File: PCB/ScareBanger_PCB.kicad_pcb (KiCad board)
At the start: 2 copper layers, 76 x 56 mm, 15 parts, among them J1 RJ45, J16 Conn_01x10_Female - SAINSMART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, J17 Screw_Terminal_01x10 - HILETG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, J2 1757271, J3 Screw_Terminal_01x06, J4 Barrel_Jack_Switch, J6 Screw_Terminal_01x06, J7 Screw_Terminal_01x06, SW1 SW_SPDT, SW2 SW_SPDT

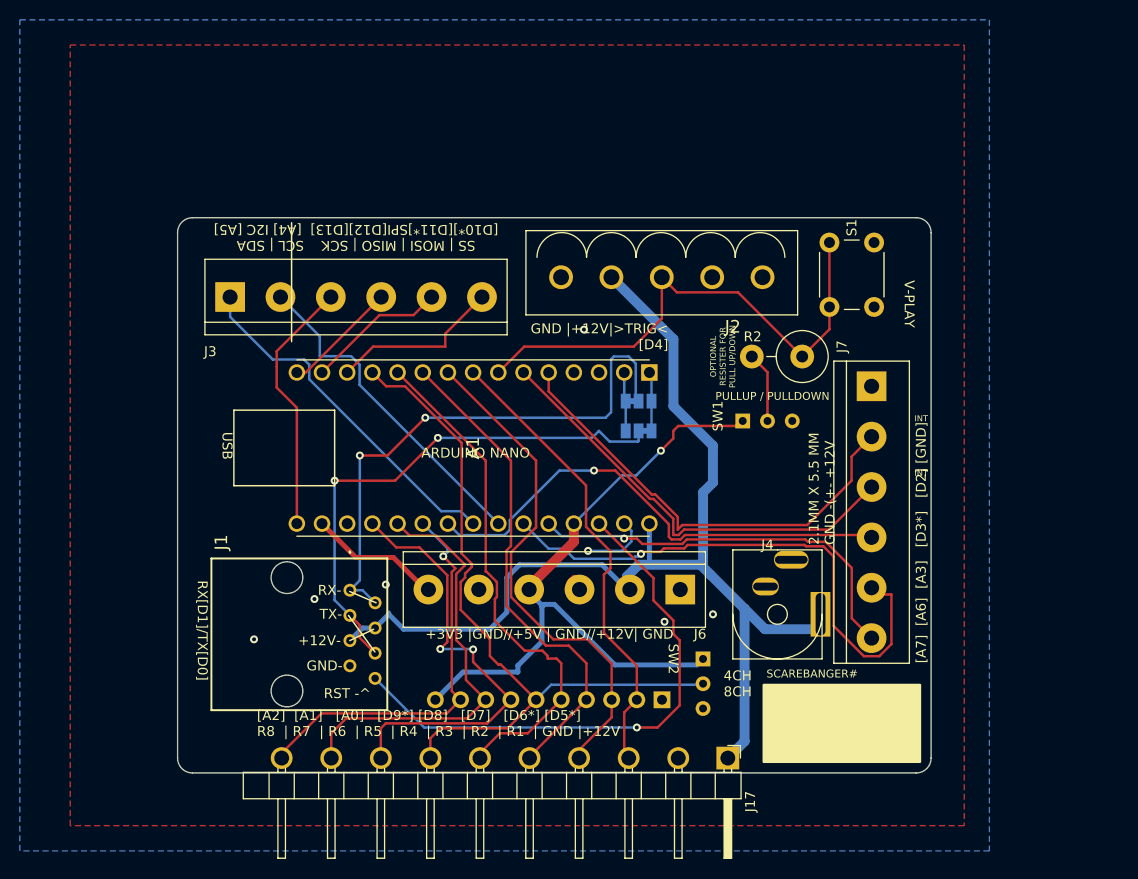
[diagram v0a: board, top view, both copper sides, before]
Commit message: add mp3 module
added mp3 module, both dfplayer and yx5300 options, re-did layout for the mp3 player and the headphone jack options.
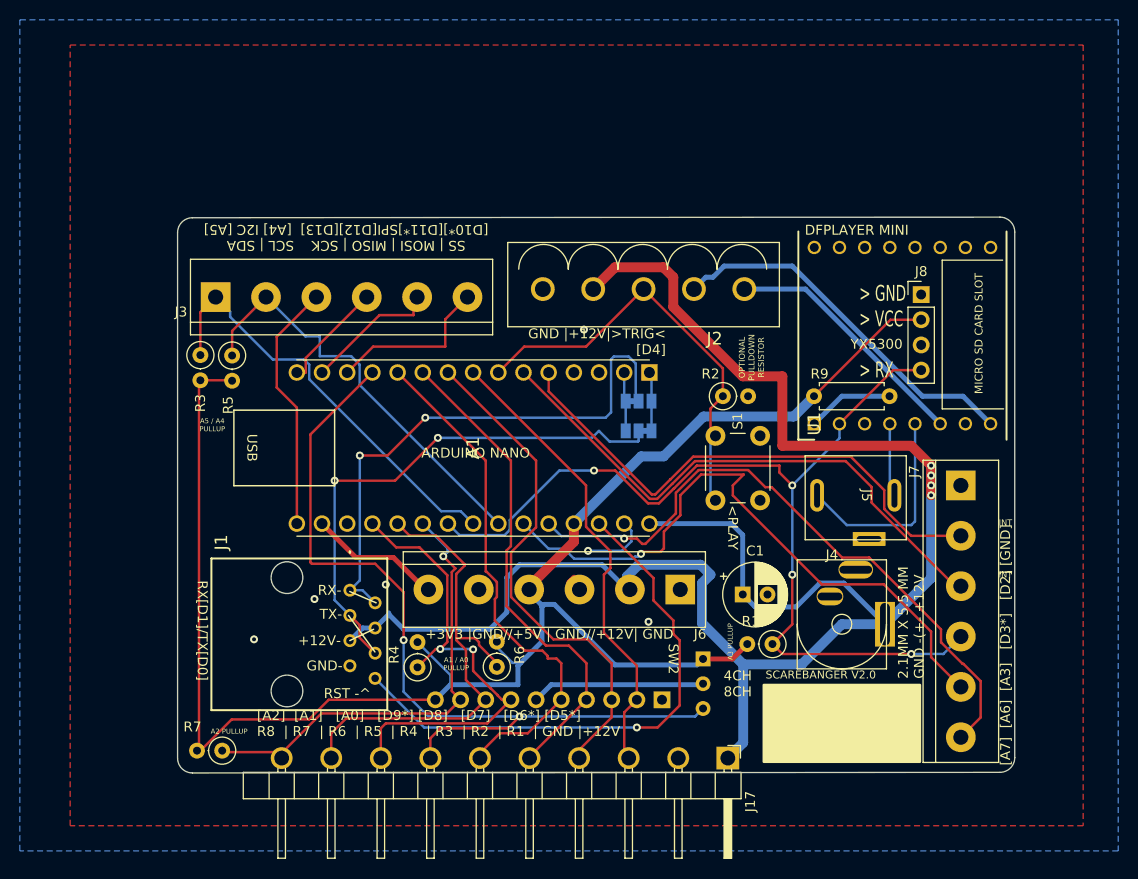
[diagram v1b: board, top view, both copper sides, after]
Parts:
- removed SW1: SW_SPDT, custom:SpDt SlideSwitch
- added C1: 180uF, Capacitor_THT:CP_Radial_D6.3mm_P2.50mm, F.Cu at (158.0, 124.0)
- added J5: AudioJack2_Ground, custom:PJ-301C HeadPhoneJack, F.Cu at (170.0, 114.0)
- added J8: Conn_01x04_Female, Connector_PinHeader_2.54mm:PinHeader_1x04_P2.54mm_Vertical, F.Cu at (176.0, 93.8)
- added R1: R, Resistor_THT:R_Axial_DIN0207_L6.3mm_D2.5mm_P2.54mm_Vertical, F.Cu at (161.0, 129.0)
- added R3: R, Resistor_THT:R_Axial_DIN0207_L6.3mm_D2.5mm_P2.54mm_Vertical, F.Cu at (103.3, 99.9)
- added R4: R, Resistor_THT:R_Axial_DIN0207_L6.3mm_D2.5mm_P2.54mm_Vertical, F.Cu at (125.2, 131.3)
- added R5: R, Resistor_THT:R_Axial_DIN0207_L6.3mm_D2.5mm_P2.54mm_Vertical, F.Cu at (106.5, 99.9)
- added R6: R, Resistor_THT:R_Axial_DIN0207_L6.3mm_D2.5mm_P2.54mm_Vertical, F.Cu at (133.2, 131.3)
- added R7: R, Resistor_THT:R_Axial_DIN0207_L6.3mm_D2.5mm_P2.54mm_Vertical, F.Cu at (105.5, 139.8)
- added R9: 1K, Resistor_THT:R_Axial_DIN0207_L6.3mm_D2.5mm_P7.62mm_Horizontal, F.Cu at (165.2, 104.0)
- added U1: DFR0299, SamacSys_Parts:DIPS1778W50P254L2100H170Q16N, F.Cu at (165.2, 106.8)
- R2: footprint Resistor_THT:R_Axial_DIN0516_L15.5mm_D5.0mm_P5.08mm_Vertical -> Resistor_THT:R_Axial_DIN0207_L6.3mm_D2.5mm_P2.54mm_Vertical
- moved S1 22.6 mm to (155.2, 114.5)
- moved J7 13.5 mm to (180.0, 113.0)
- moved R2 8.94 mm to (156.0, 104.0), turned to 0 degrees
- moved J4 6.58 mm to (168.0, 127.0)
- moved J2 2.19 mm to (158.2, 93.2)
- moved J3 1.46 mm to (104.8, 94.0)
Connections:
- J16 pad 6: Net-(A1-Pad12) -> Net-(J16-Pad6)
- R2 pad 2: Net-(R2-Pad2) -> GND
- SW2 pad 2: Net-(A1-Pad12) -> Net-(J16-Pad6)
- SW2 pad 3: unconnected-(SW2-Pad3) -> Net-(A1-Pad12)
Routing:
- net +5V: track 69.1 -> 172.4 mm, vias 1 -> 0
- net +12V: track 112.9 -> 186.9 mm, vias 0 -> 4
- net Net-(A1-Pad22): track 50.4 -> 98.3 mm, vias 1 -> 4
- net SPKR -: track 0.00 -> 37.5 mm
- net SPKR +: track 0.00 -> 25.4 mm
- net Net-(A1-Pad26): track 40.7 -> 64.8 mm
- net Net-(J5-Pad3): track 0.00 -> 21.1 mm
- net Net-(J16-Pad6): track 0.00 -> 17.5 mm
- net Net-(A1-Pad6): track 44.9 -> 57.1 mm
- net Net-(A1-Pad12): track 73.3 -> 85.0 mm, vias 0 -> 2
- net Net-(A1-Pad7): track 53.0 -> 43.0 mm
- net Net-(A1-Pad24): track 33.8 -> 42.6 mm
- net Net-(R9-Pad2): track 0.00 -> 8.74 mm
- net Net-(A1-Pad25): track 55.7 -> 64.4 mm
- net Net-(A1-Pad5): track 46.3 -> 53.9 mm
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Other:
- board size 76 x 56 mm -> 84.4 x 56.1 mm
- board text added: "<PLAY"
- board text added: "> GND > VCC > RX"
- board text added: "A1 / A0 PULLUP"
- board text added: "A2 PULLUP"
- board text added: "A3 PULLUP"
- board text added: "A5 / A4 PULLUP"
- board text added: "DFPLAYER MINI"
- board text added: "IF CONNECTING MULTIPLE BOARDS TO SAME TRIGGER HAVE THEM ALL SHARE THE SAME POWER SUPPLY"
- board text added: "OPTIONAL PULLDOWN RESISTOR"
- board text added: "SCAREBANGER V2.0"
- board text added: "ScareBanger Board 2022/10/09"
- board text added: "YX5300"
- board text removed: "OPTIONAL RESISTER FOR PULL UP/DOWN"
- board text removed: "PULLUP / PULLDOWN"
- board text removed: "SCAREBANGER#"
- board text removed: "ScareBanger Board 2022/10/02"
- board text removed: "V-PLAY"
- board text removed: "V2.0"

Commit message: ADDED MOUNTING HOLES
ADDED 2 MOUNTING HOLES TO BOARD.
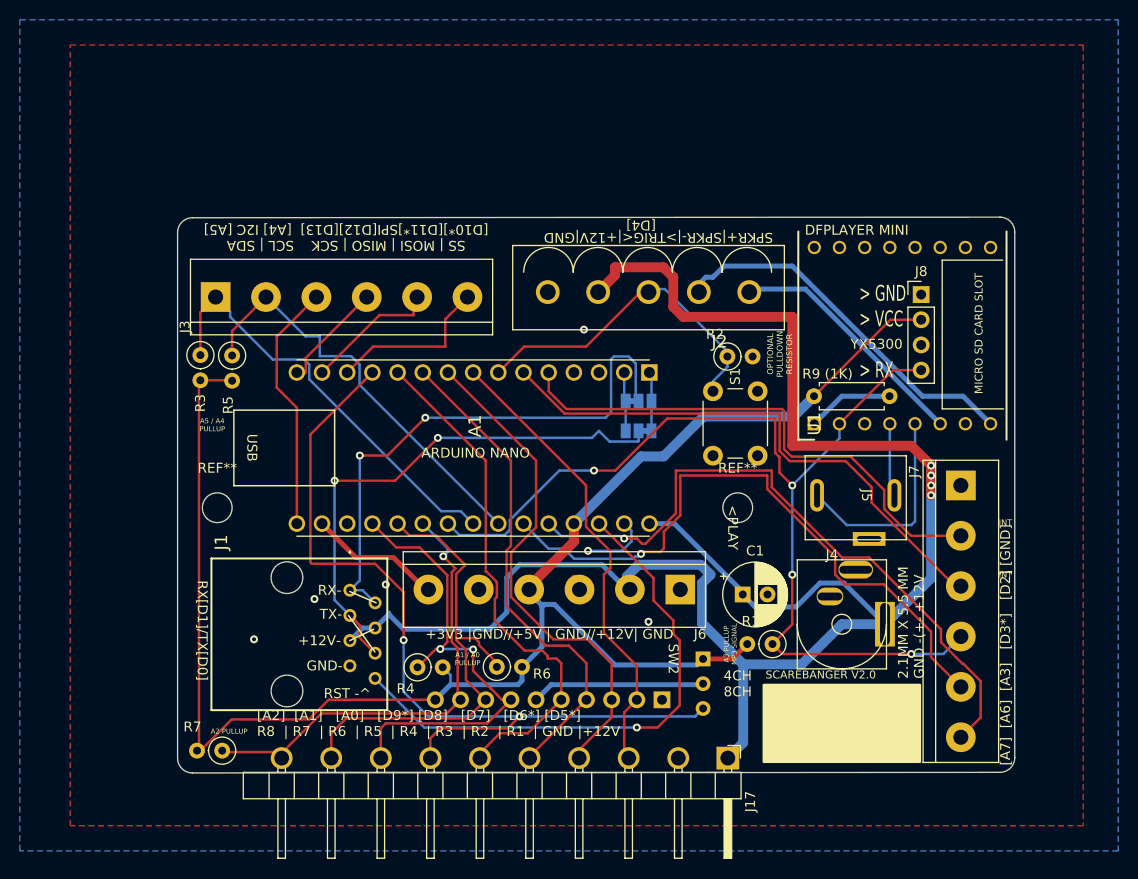
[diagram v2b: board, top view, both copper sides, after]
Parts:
- added REF**: MountingHole_3mm, MountingHole:MountingHole_3mm, F.Cu at (105.0, 115.2)
- added REF**: MountingHole_3mm, MountingHole:MountingHole_3mm, F.Cu at (157.5, 115.2)
- R9 (1K): renamed from R9
- moved S1 4.51 mm to (155.0, 110.0)
- moved R2 4.03 mm to (156.5, 100.0)
- moved J2 0.59 mm to (158.7, 93.5)
- turned R4 to 0 degrees
- turned R6 to 0 degrees
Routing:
- net Net-(A1-Pad7): track 43.0 -> 32.8 mm
- net +5V: track 172.4 -> 165.9 mm
- net Net-(A1-Pad22): track 98.3 -> 102.0 mm
- net Net-(A1-Pad26): track 64.8 -> 67.0 mm
- net Net-(A1-Pad6): track 57.1 -> 56.2 mm
- net Net-(A1-Pad5): track 53.9 -> 52.9 mm
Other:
- board text added: "A3 PULLUP MP3 SIGNAL"
- board text added: "SPKR+|SPKR-|>TRIG<|+12V|GND"
- board text added: "[D4]"
- board text removed: "A3 PULLUP"
- board text removed: "GND |+12V|>TRIG< [D4]"
